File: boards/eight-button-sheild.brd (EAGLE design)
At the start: 53.3 x 63.5 mm, 11 parts, among them J4 ARDUINO_R3_SHIELD, SW1 BUTTON, SW2 BUTTON, SW3 BUTTON, SW4 BUTTON, SW5 BUTTON, SW6 BUTTON, SW7 BUTTON, SW8 BUTTON

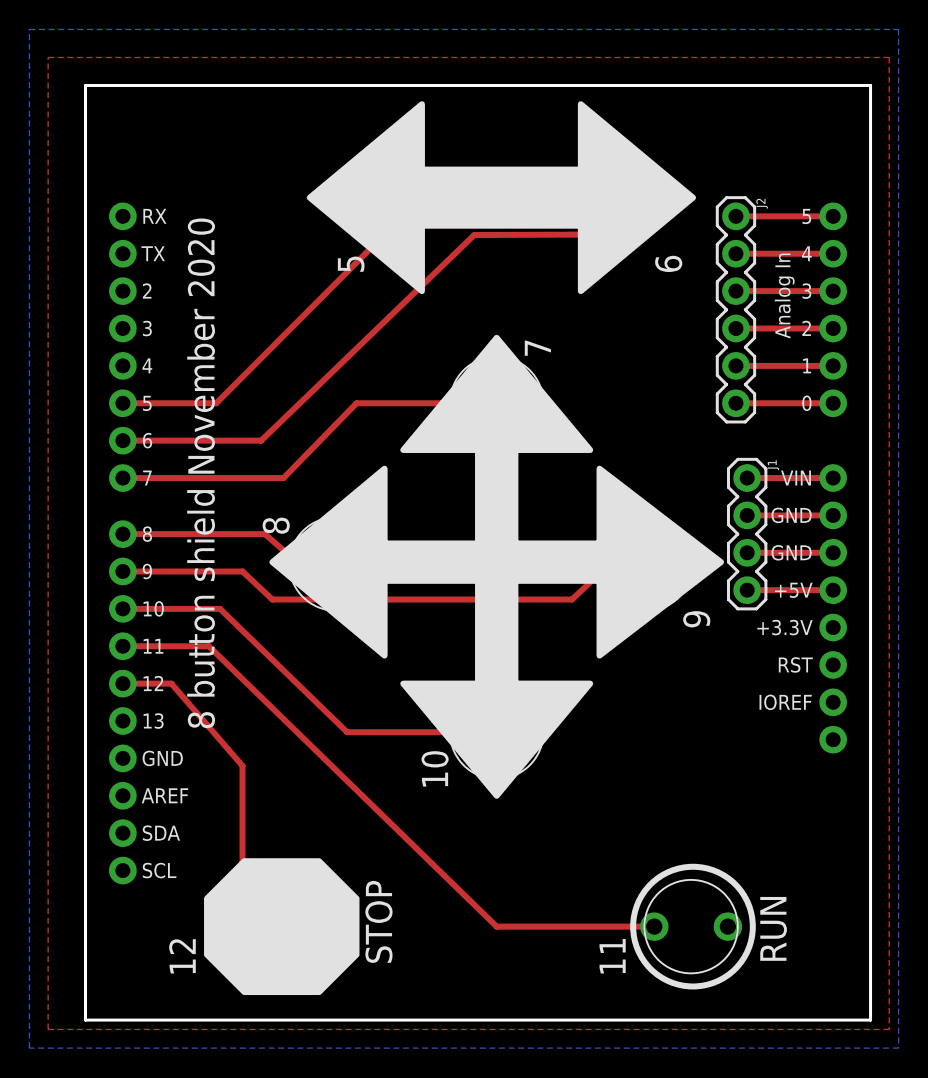
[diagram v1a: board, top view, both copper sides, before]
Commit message: xyz stepper control
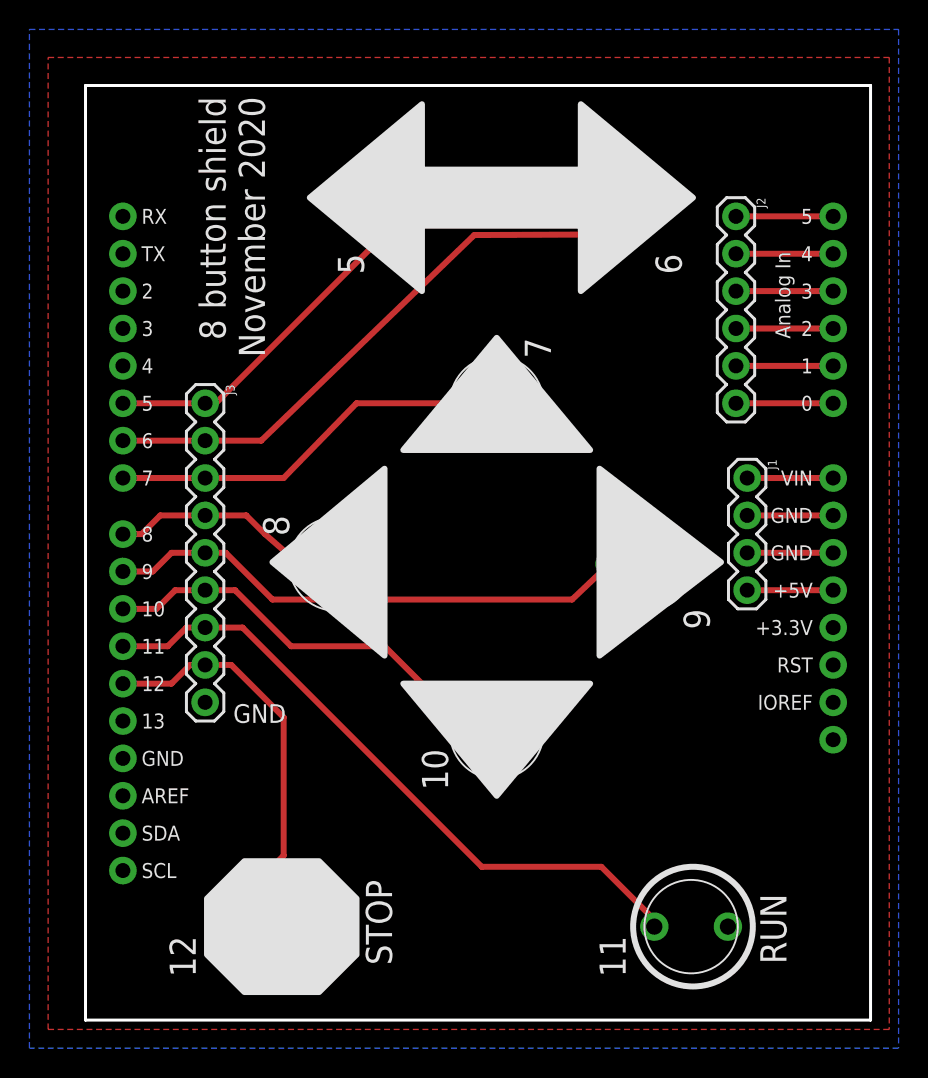
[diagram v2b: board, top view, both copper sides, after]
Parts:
- added J3: (no value), SparkFun-Connectors:1X09
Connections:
- net GND: now also J3.9
- net N$1: now also J3.1
- net N$10: now also J3.7
- net N$11: now also J3.8
- net N$4: now also J3.2
- net N$5: now also J3.3
- net N$6: now also J3.4
- net N$7: now also J3.5
- net N$8: now also J3.6
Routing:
- net N$11: track 21.6 -> 28.3 mm
- net N$8: track 26.3 -> 27.8 mm
- net N$10: track 43.9 -> 45.3 mm
- net N$7: track 34.8 -> 35.9 mm
- net N$6: track 12.7 -> 13.8 mm
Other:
- board text added: "GND"
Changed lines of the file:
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@@
-</polygon>
-<polygon width="0.4064" layer="21">
-<vertex x="20.32" y="32.385"/>
-<vertex x="34.925" y="32.385"/>
-<vertex x="34.925" y="29.845"/>
-<vertex x="20.32" y="29.845"/>
-</polygon>
-<polygon width="0.4064" layer="21">
-<vertex x="26.67" y="38.735"/>
-<vertex x="29.21" y="38.735"/>
-<vertex x="29.21" y="22.86"/>
-<vertex x="26.67" y="22.86"/>
 </polygon>
 <polygon width="0.4064" layer="21">
@@
 <text x="47.625" y="3.81" size="1.778" layer="21" rot="R90">RUN</text>
 <text x="19.05" y="9.525" size="1.778" layer="21" rot="R270">STOP</text>
-<text x="6.985" y="54.61" size="1.778" layer="21" rot="R270">8 button shield November 2020</text>
+<text x="7.747" y="62.738" size="1.778" layer="21" rot="R270">8 button shield
+November 2020</text>
 <text x="5.715" y="5.715" size="1.778" layer="21" rot="R270">12</text>
 <text x="34.925" y="5.715" size="1.778" layer="21" rot="R270">11</text>
@@
 <text x="17.145" y="52.07" size="1.778" layer="21" rot="R270">5</text>
 <circle x="41.275" y="6.35" radius="4.06598125" width="0.4064" layer="21"/>
+<text x="10.033" y="20.193" size="1.27" layer="21">GND</text>
 </plain>
 <attributes>
@@
 <attribute name="PROD_ID" value="CONN-08437" x="44.196" y="54.61" size="1.778" layer="27" rot="R270" display="off"/>
 </element>
+<element name="J3" library="SparkFun-Connectors" package="1X09" value="" x="8.128" y="41.91" rot="R270"/>
 </elements>
 <signals>
@@
 <wire x1="50.8" y1="34.29" x2="44.958" y2="34.29" width="0.4064" layer="1"/>
 <wire x1="44.958" y1="31.75" x2="50.8" y2="31.75" width="0.4064" layer="1"/>
+<contactref element="J3" pad="9"/>
 </signal>
 <signal name="N$30">
@@
 <contactref element="J4" pad="D5"/>
 <contactref element="SW1" pad="P$1"/>
-<wire x1="2.54" y1="41.91" x2="8.89" y2="41.91" width="0.4064" layer="1"/>
-<wire x1="8.89" y1="41.91" x2="20.32" y2="53.380640625" width="0.4064" layer="1"/>
+<contactref element="J3" pad="1"/>
+<wire x1="2.54" y1="41.91" x2="8.128" y2="41.91" width="0.4064" layer="1"/>
+<wire x1="20.32" y1="53.380640625" x2="8.849359375" y2="41.91" width="0.4064" layer="1"/>
+<wire x1="8.849359375" y1="41.91" x2="8.128" y2="41.91" width="0.4064" layer="1"/>
 </signal>
 <signal name="N$4">
 <contactref element="J4" pad="D6"/>
 <contactref element="SW2" pad="P$1"/>
-<wire x1="2.54" y1="39.37" x2="11.938" y2="39.37" width="0.4064" layer="1"/>
 <wire x1="26.416" y1="53.34" x2="36.068" y2="53.380640625" width="0.4064" layer="1"/>
 <wire x1="11.938" y1="39.37" x2="26.416" y2="53.34" width="0.4064" layer="1"/>
+<contactref element="J3" pad="2"/>
+<wire x1="2.54" y1="39.37" x2="8.128" y2="39.37" width="0.4064" layer="1"/>
+<wire x1="8.128" y1="39.37" x2="11.938" y2="39.37" width="0.4064" layer="1"/>
 </signal>
 <signal name="N$5">
 <contactref element="J4" pad="D7"/>
 <contactref element="SW3" pad="P$1"/>
-<wire x1="2.54" y1="36.83" x2="13.462" y2="36.83" width="0.4064" layer="1"/>
 <wire x1="13.462" y1="36.83" x2="18.415" y2="41.91" width="0.4064" layer="1"/>
 <wire x1="18.415" y1="41.91" x2="25.440640625" y2="41.91" width="0.4064" layer="1"/>
+<contactref element="J3" pad="3"/>
+<wire x1="2.54" y1="36.83" x2="8.128" y2="36.83" width="0.4064" layer="1"/>
+<wire x1="8.128" y1="36.83" x2="13.462" y2="36.83" width="0.4064" layer="1"/>
 </signal>
 <signal name="N$6">
 <contactref element="J4" pad="D8"/>
 <contactref element="SW4" pad="P$1"/>
-<wire x1="2.54" y1="33.02" x2="12.192" y2="33.02" width="0.4064" layer="1"/>
 <wire x1="12.192" y1="33.02" x2="14.518640625" y2="30.988" width="0.4064" layer="1"/>
+<contactref element="J3" pad="4"/>
+<wire x1="2.54" y1="33.02" x2="3.81" y2="33.02" width="0.4064" layer="1"/>
+<wire x1="3.81" y1="33.02" x2="5.08" y2="34.29" width="0.4064" layer="1"/>
+<wire x1="5.08" y1="34.29" x2="8.128" y2="34.29" width="0.4064" layer="1"/>
+<wire x1="8.128" y1="34.29" x2="10.922" y2="34.29" width="0.4064" layer="1"/>
+<wire x1="10.922" y1="34.29" x2="12.192" y2="33.02" width="0.4064" layer="1"/>
 </signal>
 <signal name="N$7">
 <contactref element="J4" pad="D9"/>
 <contactref element="SW5" pad="P$1"/>
-<wire x1="2.54" y1="30.48" x2="10.668" y2="30.48" width="0.4064" layer="1"/>
-<wire x1="10.668" y1="30.48" x2="12.7" y2="28.575" width="0.4064" layer="1"/>
 <wire x1="12.7" y1="28.575" x2="33.060640625" y2="28.575" width="0.4064" layer="1"/>
 <wire x1="33.060640625" y1="28.575" x2="35.600640625" y2="30.988" width="0.4064" layer="1"/>
+<contactref element="J3" pad="5"/>
+<wire x1="2.54" y1="30.48" x2="4.572" y2="30.48" width="0.4064" layer="1"/>
+<wire x1="4.572" y1="30.48" x2="5.842" y2="31.75" width="0.4064" layer="1"/>
+<wire x1="5.842" y1="31.75" x2="8.128" y2="31.75" width="0.4064" layer="1"/>
+<wire x1="8.128" y1="31.75" x2="9.525" y2="31.75" width="0.4064" layer="1"/>
+<wire x1="9.525" y1="31.75" x2="12.7" y2="28.575" width="0.4064" layer="1"/>
 </signal>
 <signal name="N$8">
 <contactref element="J4" pad="D10"/>
 <contactref element="SW6" pad="P$1"/>
-<wire x1="2.54" y1="27.94" x2="9.144" y2="27.94" width="0.4064" layer="1"/>
-<wire x1="9.144" y1="27.94" x2="17.78" y2="19.558" width="0.4064" layer="1"/>
-<wire x1="17.78" y1="19.558" x2="25.440640625" y2="19.558" width="0.4064" layer="1"/>
+<contactref element="J3" pad="6"/>
+<wire x1="2.54" y1="27.94" x2="4.826" y2="27.94" width="0.4064" layer="1"/>
+<wire x1="4.826" y1="27.94" x2="6.096" y2="29.21" width="0.4064" layer="1"/>
+<wire x1="6.096" y1="29.21" x2="8.128" y2="29.21" width="0.4064" layer="1"/>
+<wire x1="8.128" y1="29.21" x2="10.16" y2="29.21" width="0.4064" layer="1"/>
+<wire x1="13.97" y1="25.4" x2="20.32" y2="25.4" width="0.4064" layer="1"/>
+<wire x1="20.32" y1="25.4" x2="25.440640625" y2="20.279359375" width="0.4064" layer="1"/>
+<wire x1="25.440640625" y1="20.279359375" x2="25.440640625" y2="19.558" width="0.4064" layer="1"/>
+<wire x1="10.16" y1="29.21" x2="13.97" y2="25.4" width="0.4064" layer="1"/>
 </signal>
 <signal name="N$10">
 <contactref element="SW7" pad="P$1"/>
 <contactref element="J4" pad="D11"/>
-<wire x1="2.54" y1="25.4" x2="8.382" y2="25.4" width="0.4064" layer="1"/>
-<wire x1="8.382" y1="25.4" x2="27.94" y2="6.35" width="0.4064" layer="1"/>
-<wire x1="27.94" y1="6.35" x2="38.648640625" y2="6.35" width="0.4064" layer="1"/>
+<contactref element="J3" pad="7"/>
+<wire x1="2.54" y1="25.4" x2="5.588" y2="25.4" width="0.4064" layer="1"/>
+<wire x1="5.588" y1="25.4" x2="6.858" y2="26.67" width="0.4064" layer="1"/>
+<wire x1="6.858" y1="26.67" x2="8.128" y2="26.67" width="0.4064" layer="1"/>
+<wire x1="8.128" y1="26.67" x2="10.668" y2="26.67" width="0.4064" layer="1"/>
+<wire x1="38.648640625" y1="6.817359375" x2="38.648640625" y2="6.35" width="0.4064" layer="1"/>
+<wire x1="10.668" y1="26.67" x2="26.924" y2="10.414" width="0.4064" layer="1"/>
+<wire x1="26.924" y1="10.414" x2="35.052" y2="10.414" width="0.4064" layer="1"/>
+<wire x1="35.052" y1="10.414" x2="38.648640625" y2="6.817359375" width="0.4064" layer="1"/>
 </signal>
 <signal name="N$11">
 <contactref element="SW8" pad="P$1"/>
 <contactref element="J4" pad="D12"/>
+<contactref element="J3" pad="8"/>
 <wire x1="2.54" y1="22.86" x2="5.842" y2="22.86" width="0.4064" layer="1"/>
-<wire x1="5.842" y1="22.86" x2="10.668" y2="17.272" width="0.4064" layer="1"/>
-<wire x1="10.668" y1="17.272" x2="10.668" y2="6.35" width="0.4064" layer="1"/>
-<wire x1="10.668" y1="6.35" x2="10.708640625" y2="6.35" width="0.4064" layer="1"/>
+<wire x1="5.842" y1="22.86" x2="7.112" y2="24.13" width="0.4064" layer="1"/>
+<wire x1="7.112" y1="24.13" x2="8.128" y2="24.13" width="0.4064" layer="1"/>
+<wire x1="8.128" y1="24.13" x2="9.906" y2="24.13" width="0.4064" layer="1"/>
+<wire x1="9.906" y1="24.13" x2="13.462" y2="20.574" width="0.4064" layer="1"/>
+<wire x1="13.462" y1="20.574" x2="13.462" y2="11.176" width="0.4064" layer="1"/>
+<wire x1="13.462" y1="11.176" x2="10.668" y2="8.382" width="0.4064" layer="1"/>
+<wire x1="10.668" y1="8.382" x2="10.668" y2="6.390640625" width="0.4064" layer="1"/>
+<wire x1="10.668" y1="6.390640625" x2="10.708640625" y2="6.35" width="0.4064" layer="1"/>
 </signal>
 <signal name="N$9">
@@
 </board>
 </drawing>
+<compatibility>
+<note version="6.3" minversion="6.2.2" severity="warning">
+Since Version 6.2.2 text objects can contain more than one line,
+which will not be processed correctly with this version.
+</note>
+</compatibility>
 </eagle>
